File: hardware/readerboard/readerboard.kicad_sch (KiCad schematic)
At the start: 65 parts, among them J1 Screw_Terminal_01x08, J3 RESET, J3 RESET DISABLE (Remove to prog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, J4 EEPROM VOLTAGE, Q0 FQP47P06, U0 74HCT238, U1 ULN2803A*, U11 THVD1439, U12 74HCT238, U13 74HCT238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

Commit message: wip
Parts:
- J4: value EEPROM VOLTAGE -> LOGIC VOLTAGE
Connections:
- net +5V: no longer C9.1, R32.1, R34.1, U11.8 (VCC)
- net V_{LOGIC}: now reaches J4.2 (C), R52.1, R53.1, U16.8 (VCC)
- net V_{LOGIC}: now also C9.1, R32.1, R34.1, U11.8 (VCC)
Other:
- note added: "29-SEP-2024"
- note removed: "16-SEP-2024"
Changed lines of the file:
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@@
 	(wire
 		(pts
+			(xy 212.09 163.83) (xy 212.09 166.37)
+		)
+		(stroke
+			(width 0)
+			(type default)
+		)
+	)
+	(wire
+		(pts
 			(xy 243.205 135.89) (xy 251.46 135.89)
 		)
@@
 		)
 	)
-	(text "16-SEP-2024"
+	(text "29-SEP-2024"
 		(exclude_from_sim no)
 		(at 342.9 263.525 0)
@@
 	)
 	(symbol
+		(lib_id "power:+5V")
+		(at 212.09 163.83 0)
+		(unit 1)
+		(exclude_from_sim no)
+		(in_bom yes)
+		(on_board yes)
+		(dnp no)
+		(fields_autoplaced yes)
+		(property "Reference" "#PWR027"
+			(at 212.09 167.64 0)
+			(effects
+				(font
+					(size 1.27 1.27)
+				)
+				(hide yes)
+			)
+		)
+		(property "Value" "V_{LOGIC}"
+			(at 212.09 158.75 0)
+			(effects
+				(font
+					(size 1.27 1.27)
+				)
+			)
+		)
+		(property "Footprint" ""
+			(at 212.09 163.83 0)
+			(effects
+				(font
+					(size 1.27 1.27)
+				)
+				(hide yes)
+			)
+		)
+		(property "Datasheet" ""
+			(at 212.09 163.83 0)
+			(effects
+				(font
+					(size 1.27 1.27)
+				)
+				(hide yes)
+			)
+		)
+		(property "Description" ""
+			(at 212.09 163.83 0)
+			(effects
+				(font
+					(size 1.27 1.27)
+				)
+				(hide yes)
+			)
+		)
+		(pin "1"
+		)
+		(instances
+			(project "readerboard"
+				(path "/68206880-187a-441b-ad1d-285a8d6fa444"
+					(reference "#PWR027")
+					(unit 1)
+				)
+			)
+		)
+	)
+	(symbol
 		(lib_id "power:+9V")
 		(at 161.29 107.95 0)
@@
 		(on_board yes)
 		(dnp no)
-		(fields_autoplaced yes)
 		(property "Reference" "#PWR014"
 			(at 246.38 196.088 0)
@@
 			)
 		)
-		(property "Value" "+5V"
-			(at 246.38 187.833 0)
+		(property "Value" "V_{LOGIC}"
+			(at 243.332 187.96 0)
 			(effects
 				(font
 					(size 1.27 1.27)
 				)
+				(justify left)
 			)
 		)
@@
 			)
 		)
-		(property "Value" "EEPROM VOLTAGE"
+		(property "Value" "LOGIC VOLTAGE"
 			(at 181.61 161.29 0)
 			(effects

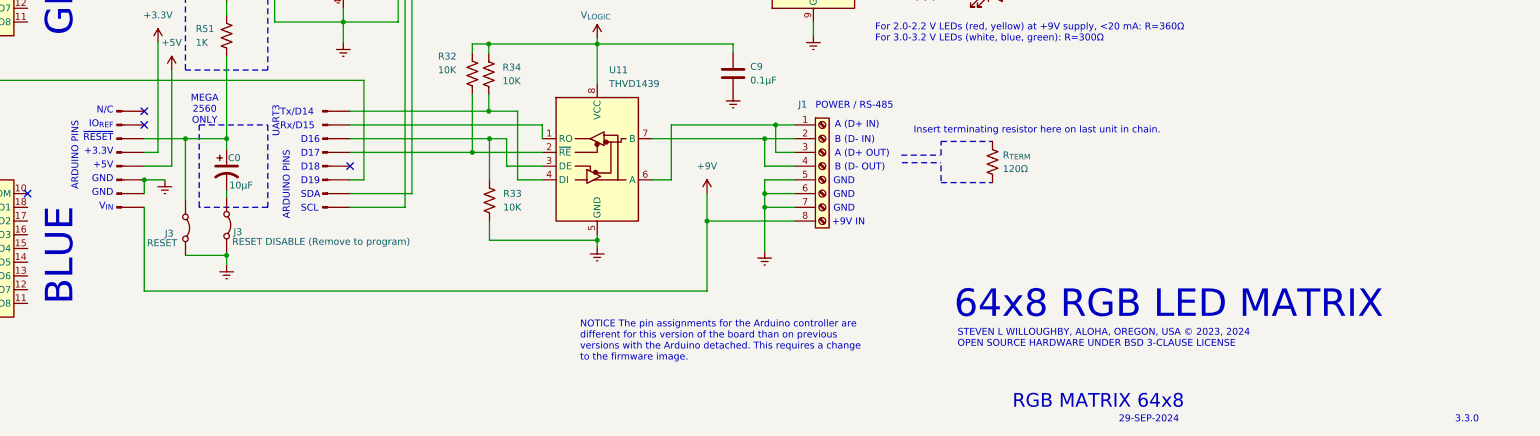
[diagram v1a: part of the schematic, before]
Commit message: pcb 3.3.1 updates, documentation
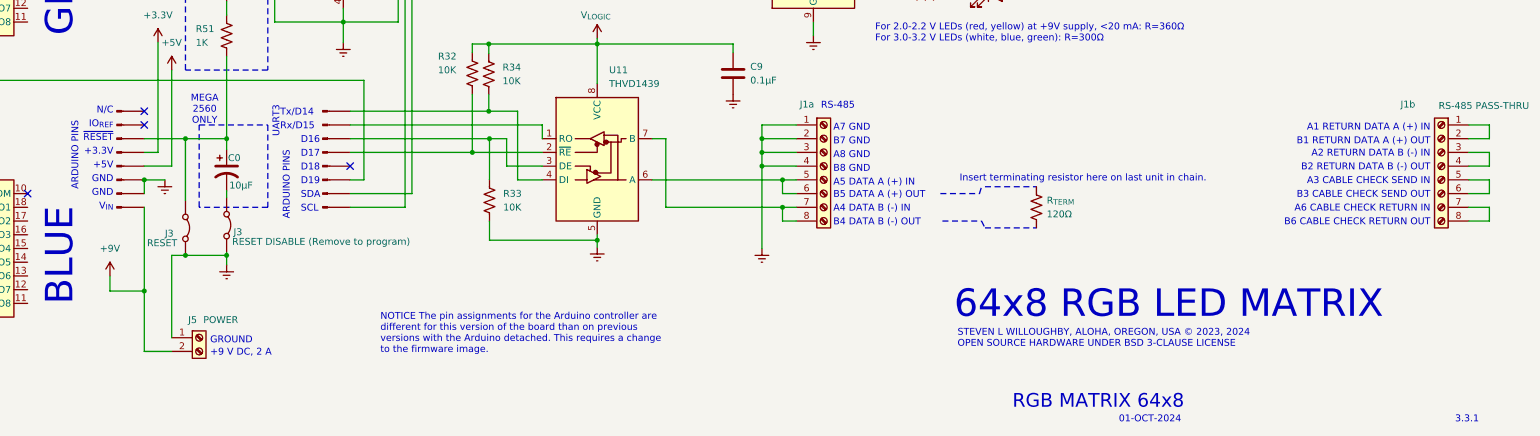
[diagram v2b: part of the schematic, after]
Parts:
- added J1b: RS-485 PASS-THRU, symbol Connector:Screw_Terminal_01x08
- added J5: POWER, symbol Connector:Screw_Terminal_01x02
- renumbered J1 to J1a
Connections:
- net +9V: now also J5.2 (Pin_2); no longer J1a.8 (Pin_8)
- net GNDREF: now also J1a.1 (Pin_1), J1a.2 (Pin_2), J1a.3 (Pin_3), J1a.4 (Pin_4), J5.1 (Pin_1); no longer J1a.5 (Pin_5), J1a.6 (Pin_6), J1a.7 (Pin_7)
- new net: J1a.5 (Pin_5), J1a.6 (Pin_6), U11.6 (A)
- new net: J1a.7 (Pin_7), J1a.8 (Pin_8), U11.7 (B)
- new net: J1b.1 (Pin_1), J1b.2 (Pin_2)
- new net: J1b.3 (Pin_3), J1b.4 (Pin_4)
- new net: J1b.5 (Pin_5), J1b.6 (Pin_6)
- new net: J1b.7 (Pin_7), J1b.8 (Pin_8)
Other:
- note added: "+9 V DC, 2 A"
- note added: "01-OCT-2024"
- note added: "3.3.1"
- note added: "A1 RETURN DATA A (+) IN"
- note added: "A2 RETURN DATA B (-) IN"
- note added: "A3 CABLE CHECK SEND IN"
- note added: "A4 DATA B (-) IN"
- note added: "A5 DATA A (+) IN"
- note added: "A6 CABLE CHECK RETURN IN"
- note added: "A7 GND"
- note added: "A8 GND"
- note added: "B1 RETURN DATA A (+) OUT"
- note added: "B2 RETURN DATA B (-) OUT"
- note added: "B3 CABLE CHECK SEND OUT"
- note added: "B4 DATA B (-) OUT"
- note added: "B5 DATA A (+) OUT"
- note added: "B6 CABLE CHECK RETURN OUT"
- note added: "B7 GND"
- note added: "B8 GND"
- note added: "GROUND"
- note added: "RS-485"
- note removed: "+9V IN"
- note removed: "29-SEP-2024"
- note removed: "3.3.0"
- note removed: "A (D+ IN)"
- note removed: "A (D+ OUT)"
- note removed: "B (D- IN)"
- note removed: "B (D- OUT)"
- note removed: "POWER / RS-485"
- moved on the sheet: R_{TERM}

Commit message: morse, etc
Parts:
- added J6: SPEAKER, symbol Connector:Screw_Terminal_01x02
- added LS1: 8Ω Speaker, symbol Device:Speaker
- added R54: R_US, symbol Device:R_US
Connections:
- net GNDREF: now also J6.2 (Pin_2)
- new net: J6.1 (Pin_1), R54.2
- no-connect marks 18 -> 17
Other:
- note added: "04-OCT-2024"
- note added: "220Ω (5V) 150Ω (3.3V)"
- note added: "3.4.0"
- note removed: "01-OCT-2024"
- note removed: "3.3.1"

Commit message: dimmers
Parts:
- added C13: 100μF, symbol Device:C_Polarized_US
- added Q24: 2N2222 / BC547, symbol Device:Q_NPN_CBE
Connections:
- net +9V: now also J6.1 (Pin_1)
- net GNDREF: now also Q24.3 (E); no longer J6.2 (Pin_2)
- net at J?.6 (Pin_6): now also C13.2
- net at R54.2: now also J6.2 (Pin_2), Q24.1 (C); no longer J6.1 (Pin_1)
- net at R54.1: now also C13.1, Q24.2 (B)
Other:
- note added: "08-OCT-2024"
- note added: "10K"
- note added: "3.4.1"
- note removed: "04-OCT-2024"
- note removed: "220Ω (5V) 150Ω (3.3V)"
- note removed: "3.4.0"
- moved on the sheet: R54

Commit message: design updates
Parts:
- added D520: 4A, symbol Device:D_Filled
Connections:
- net +9V: now also D520.2 (A); no longer J?.8 (Pin_8)
- new net: D520.1 (K), J?.8 (Pin_8)
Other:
- note added: "09-OCT-2024"
- note removed: "08-OCT-2024"
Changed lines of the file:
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@@
 	)
 	(junction
+		(at 162.56 250.19)
+		(diameter 0)
+		(color 0 0 0 0)
+	)
+	(junction
 		(at 282.575 128.27)
 		(diameter 0)
@@
 	)
 	(junction
-		(at 162.56 239.014)
-		(diameter 0)
-		(color 0 0 0 0)
-	)
-	(junction
 		(at 186.69 181.61)
 		(diameter 0)
@@
 	(wire
 		(pts
+			(xy 162.56 250.19) (xy 167.64 250.19)
+		)
+		(stroke
+			(width 0)
+			(type default)
+		)
+	)
+	(wire
+		(pts
 			(xy 332.74 151.13) (xy 278.13 151.13)
 		)
@@
 	(wire
 		(pts
+			(xy 162.56 243.84) (xy 162.56 250.19)
+		)
+		(stroke
+			(width 0)
+			(type default)
+		)
+	)
+	(wire
+		(pts
 			(xy 153.035 67.31) (xy 160.655 67.31)
 		)
@@
 	(wire
 		(pts
+			(xy 162.56 223.52) (xy 162.56 236.22)
+		)
+		(stroke
+			(width 0)
+			(type default)
+		)
+	)
+	(wire
+		(pts
 			(xy 111.76 241.3) (xy 120.65 241.3)
 		)
@@
 	(wire
 		(pts
-			(xy 156.21 236.22) (xy 156.21 239.014)
+			(xy 156.21 236.22) (xy 156.21 250.19)
 		)
 		(stroke
@@
 	(wire
 		(pts
-			(xy 162.56 223.52) (xy 162.56 239.014)
-		)
-		(stroke
-			(width 0)
-			(type default)
-		)
-	)
-	(wire
-		(pts
 			(xy 282.448 86.995) (xy 316.23 86.995)
 		)
@@
 	(wire
 		(pts
-			(xy 162.56 239.014) (xy 156.21 239.014)
+			(xy 156.21 250.19) (xy 162.56 250.19)
 		)
 		(stroke
@@
 	(wire
 		(pts
-			(xy 162.56 239.014) (xy 162.56 250.19)
-		)
-		(stroke
-			(width 0)
-			(type default)
-		)
-	)
-	(wire
-		(pts
 			(xy 277.495 125.095) (xy 277.495 132.08)
 		)
@@
 	(wire
 		(pts
-			(xy 167.64 250.19) (xy 162.56 250.19)
-		)
-		(stroke
-			(width 0)
-			(type default)
-		)
-	)
-	(wire
-		(pts
 			(xy 229.616 210.82) (xy 229.616 215.9)
 		)
@@
 		)
 	)
-	(text "08-OCT-2024"
+	(text "09-OCT-2024"
 		(exclude_from_sim no)
 		(at 342.9 263.525 0)
@@
 					(unit 1)
 				)
+			)
+		)
+	)
+	(symbol
+		(lib_id "Device:D_Filled")
+		(at 162.56 240.03 270)
+		(unit 1)
+		(exclude_from_sim no)
+		(in_bom yes)
+		(on_board yes)
+		(dnp no)
+		(property "Reference" "D520"
+			(at 162.56 237.49 90)
+			(effects
+				(font
+					(size 1.27 1.27)
+				)
+				(justify left)
+			)
+		)
+		(property "Value" "4A"
+			(at 162.56 242.824 90)
+			(effects
+				(font
+					(size 1.27 1.27)
+				)
+				(justify left)
+			)
+		)
+		(property "Footprint" ""
+			(at 162.56 240.03 0)
+			(effects
+				(font
+					(size 1.27 1.27)
+				)
+				(hide yes)
+			)
+		)
+		(property "Datasheet" "~"
+			(at 162.56 240.03 0)
+			(effects
+				(font
+					(size 1.27 1.27)
+				)
+				(hide yes)
+			)
+		)
+		(property "Description" "Diode, filled shape"
+			(at 162.56 240.03 0)
+			(effects
+				(font
+					(size 1.27 1.27)
+				)
+				(hide yes)
+			)
+		)
+		(property "Sim.Device" "D"
+			(at 162.56 240.03 0)
+			(effects
+				(font
+					(size 1.27 1.27)
+				)
+				(hide yes)
+			)
+		)
+		(property "Sim.Pins" "1=K 2=A"
+			(at 162.56 240.03 0)
+			(effects
+				(font
+					(size 1.27 1.27)
+				)
+				(hide yes)
+			)
+		)
+		(pin "2"
+		)
+		(pin "1"
+		)
+		(instances
+			(project ""
+				(path "/68206880-187a-441b-ad1d-285a8d6fa444"
+					(reference "D520")
+					(unit 1)
+				)

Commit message: tweaks
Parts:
- added R55: R_US, symbol Device:R_US
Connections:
- net at Q24.2 (B), R54.1: now also R55.2; no longer C13.1
- new net: C13.1, R55.1
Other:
- note added: "Optional series resistor (or jumper wire)"
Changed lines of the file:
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@@
 	(wire
 		(pts
-			(xy 332.74 151.13) (xy 278.13 151.13)
-		)
-		(stroke
-			(width 0)
-			(type default)
-		)
-	)
-	(wire
-		(pts
 			(xy 276.225 168.91) (xy 243.84 168.91)
 		)
@@
 	(wire
 		(pts
-			(xy 340.36 151.13) (xy 341.63 151.13)
-		)
-		(stroke
-			(width 0)
-			(type default)
-		)
-	)
-	(wire
-		(pts
 			(xy 62.865 134.62) (xy 62.865 124.46)
 		)
@@
 	(wire
 		(pts
+			(xy 278.13 151.13) (xy 293.37 151.13)
+		)
+		(stroke
+			(width 0)
+			(type default)
+		)
+	)
+	(wire
+		(pts
 			(xy 319.405 166.37) (xy 329.565 166.37)
 		)
@@
 	(wire
 		(pts
+			(xy 300.99 151.13) (xy 312.42 151.13)
+		)
+		(stroke
+			(width 0)
+			(type default)
+		)
+	)
+	(wire
+		(pts
 			(xy 256.54 132.08) (xy 277.495 132.08)
 		)
@@
 	(wire
 		(pts
+			(xy 320.04 151.13) (xy 341.63 151.13)
+		)
+		(stroke
+			(width 0)
+			(type default)
+		)
+	)
+	(wire
+		(pts
 			(xy 101.6 158.115) (xy 101.6 166.37)
 		)
@@
 		)
 	)
+	(text "Optional series resistor\n(or jumper wire)"
+		(exclude_from_sim no)
+		(at 317.5 146.05 0)
+		(effects
+			(font
+				(size 1.27 1.27)
+			)
+		)
+	)
 	(text "A3 CABLE CHECK SEND IN"
 		(exclude_from_sim no)
@@
 	)
 	(symbol
+		(lib_id "Device:C_Polarized_US")
+		(at 297.18 151.13 270)
+		(unit 1)
+		(exclude_from_sim no)
+		(in_bom yes)
+		(on_board yes)
+		(dnp no)
+		(property "Reference" "C13"
+			(at 297.18 144.78 90)
+			(effects
+				(font
+					(size 1.27 1.27)
+				)
+			)
+		)
+		(property "Value" "100μF"
+			(at 297.18 147.32 90)
+			(effects
+				(font
+					(size 1.27 1.27)
+				)
+			)
+		)
+		(property "Footprint" ""
+			(at 297.18 151.13 0)
+			(effects
+				(font
+					(size 1.27 1.27)
+				)
+				(hide yes)
+			)
+		)
+		(property "Datasheet" "~"
+			(at 297.18 151.13 0)
+			(effects
+				(font
+					(size 1.27 1.27)
+				)
+				(hide yes)
+			)
+		)
+		(property "Description" "Polarized capacitor, US symbol"
+			(at 297.18 151.13 0)
+			(effects
+				(font
+					(size 1.27 1.27)
+				)
+				(hide yes)
+			)
+		)
+		(pin "2"
+		)
+		(pin "1"
+		)
+		(instances
+			(project "readerboard"
+				(path "/68206880-187a-441b-ad1d-285a8d6fa444"
+					(reference "C13")
+					(unit 1)
+				)
+			)
+		)
+	)
+	(symbol
 		(lib_id "power:+9V")
 		(at 329.565 160.655 0)
@@
 	(symbol
 		(lib_id "Device:R_US")
+		(at 316.23 151.13 90)
+		(unit 1)
+		(exclude_from_sim no)
+		(in_bom yes)
+		(on_board yes)
+		(dnp no)
+		(property "Reference" "R55"
+			(at 316.23 146.05 90)
+			(effects
+				(font
+					(size 1.27 1.27)
+				)
+				(hide yes)
+			)
+		)
+		(property "Value" "R_US"
+			(at 316.23 147.32 90)
+			(effects
+				(font
+					(size 1.27 1.27)
+				)
+				(hide yes)
+			)
+		)
+		(property "Footprint" ""
+			(at 316.484 150.114 90)
+			(effects
+				(font
+					(size 1.27 1.27)
+				)
+				(hide yes)
+			)
+		)
+		(property "Datasheet" "~"
+			(at 316.23 151.13 0)
+			(effects
+				(font
+					(size 1.27 1.27)
+				)
+				(hide yes)
+			)
+		)
+		(property "Description" ""
+			(at 316.23 151.13 0)
+			(effects
+				(font
+					(size 1.27 1.27)
+				)
+				(hide yes)
+			)
+		)
+		(pin "1"
+		)
+		(pin "2"
+		)
+		(instances
+			(project "readerboard"
+				(path "/68206880-187a-441b-ad1d-285a8d6fa444"
+					(reference "R55")
+					(unit 1)
+				)
+			)
+		)
+	)
+	(symbol
+		(lib_id "Device:R_US")
 		(at 226.314 198.882 0)
 		(unit 1)
@@
 					(unit 1)
 				)
-			)
-		)
-	)
-	(symbol
-		(lib_id "Device:C_Polarized_US")
-		(at 336.55 151.13 270)
-		(unit 1)
-		(exclude_from_sim no)
-		(in_bom yes)
-		(on_board yes)
-		(dnp no)
-		(property "Reference" "C13"
-			(at 336.55 144.78 90)
-			(effects
-				(font
-					(size 1.27 1.27)
-				)
-			)
-		)
-		(property "Value" "100μF"
-			(at 336.55 147.32 90)
-			(effects
-				(font
-					(size 1.27 1.27)
-				)
-			)
-		)
-		(property "Footprint" ""
-			(at 336.55 151.13 0)
-			(effects
-				(font
-					(size 1.27 1.27)
-				)
-				(hide yes)
-			)
-		)
-		(property "Datasheet" "~"
-			(at 336.55 151.13 0)
-			(effects
-				(font
-					(size 1.27 1.27)
-				)
-				(hide yes)
-			)
-		)
-		(property "Description" "Polarized capacitor, US symbol"
-			(at 336.55 151.13 0)
-			(effects
-				(font
-					(size 1.27 1.27)
-				)
-				(hide yes)
-			)
-		)
-		(pin "2"
-		)
-		(pin "1"
-		)
-		(instances
-			(project ""
-				(path "/68206880-187a-441b-ad1d-285a8d6fa444"
-					(reference "C13")
-					(unit 1)
-				)
